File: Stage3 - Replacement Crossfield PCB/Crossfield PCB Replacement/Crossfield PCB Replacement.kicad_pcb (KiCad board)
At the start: 2 copper layers, 29 parts, among them P16-2 Power Amp Right, P25-2 Power Amp Left, P4-P24 Switch Mode PSU, P6-P18 12_Way_8-215079-2, Q1 BC549, Q2 BC549, Q3 BC549, Q4 BC549

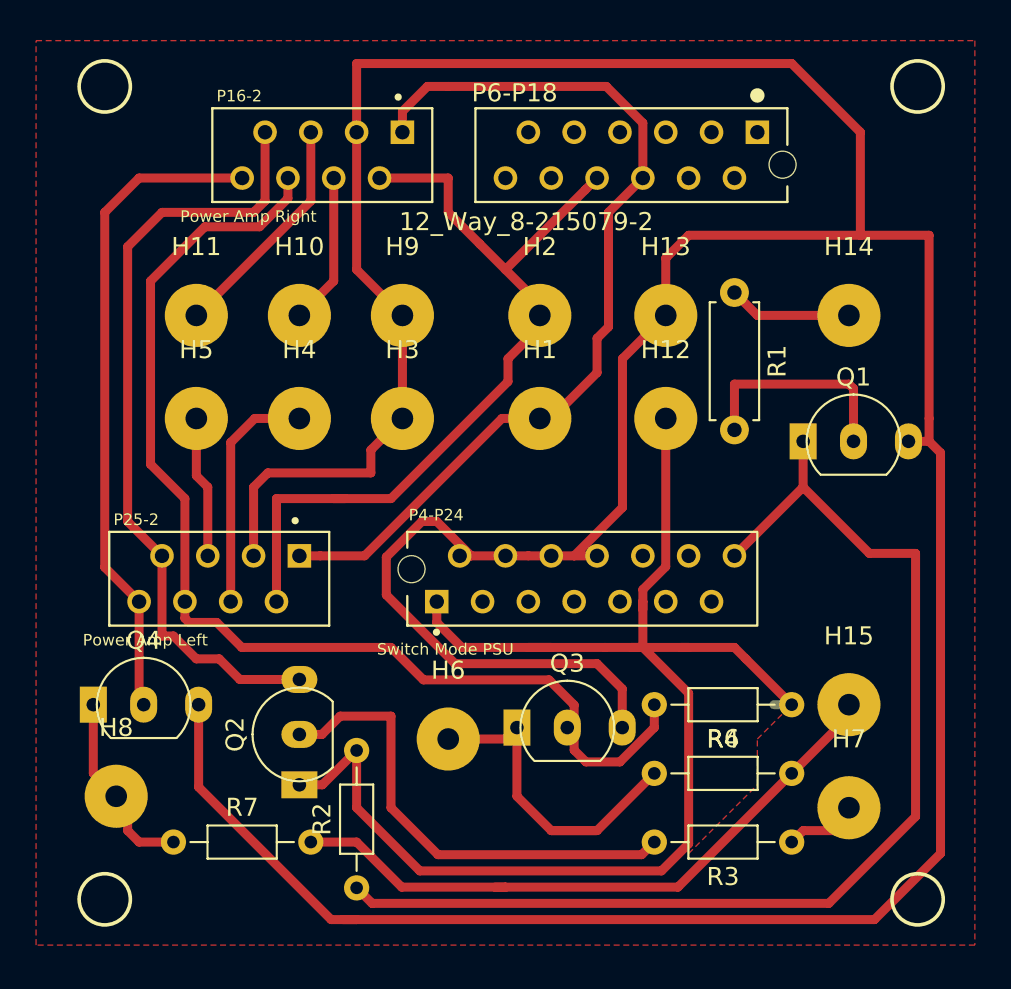
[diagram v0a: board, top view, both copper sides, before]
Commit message: Changed PCB now has USB PSU
The B&O PSU failed to provide enough mA for the raspberry. Now the switchmode PSU has been removed and replaced with a standard USB brick.
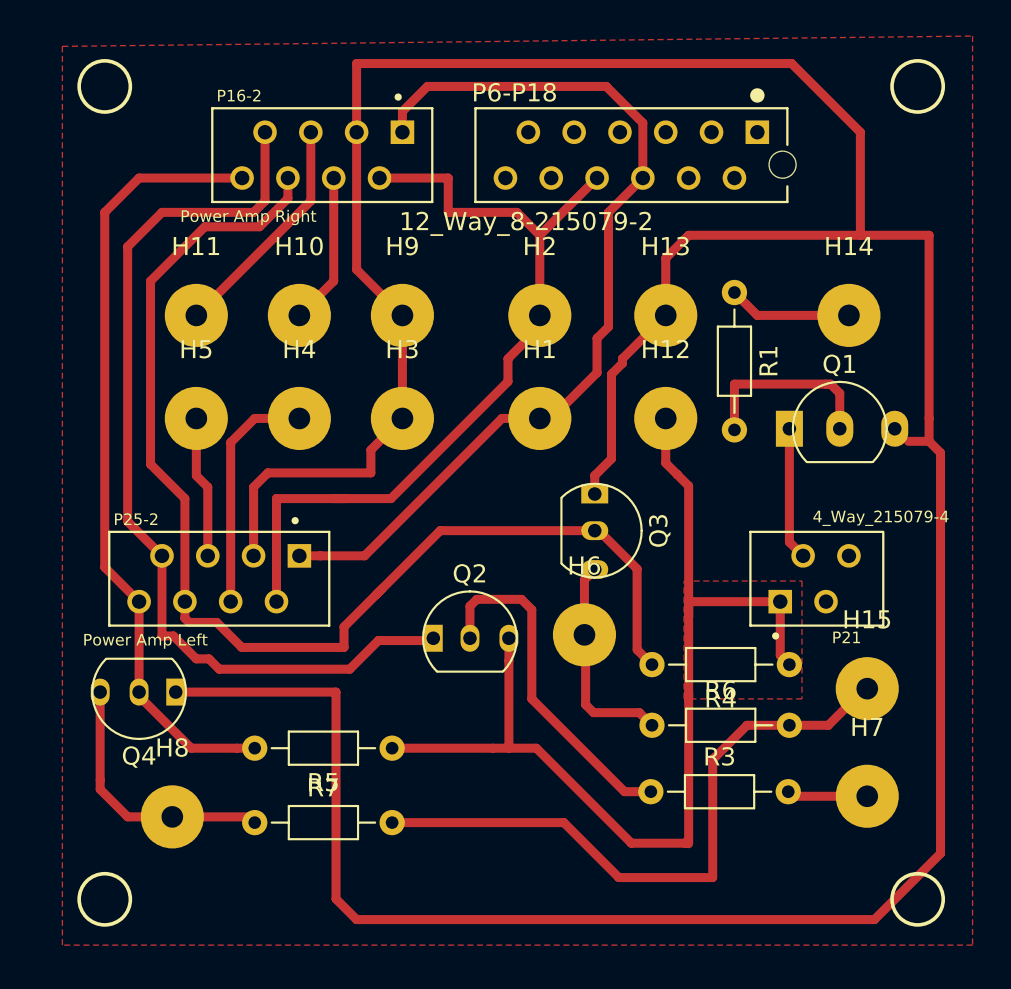
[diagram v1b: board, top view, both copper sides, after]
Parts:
- removed P4-P24: Switch Mode PSU, Connector_TE_215079_Series:TE_1-215079-4
- removed R2: 10k, Resistor_THT:R_Axial_DIN0204_L3.6mm_D1.6mm_P7.62mm_Horizontal
- added P21: 4_Way_215079-4, Connector_TE_215079_Series:TE_215079-4, F.Cu at (172.1, 109.9)
- added R5: 10k, Resistor_THT:R_Axial_DIN0204_L3.6mm_D1.6mm_P7.62mm_Horizontal, F.Cu at (146.1, 119.3)
- H6: value PLIM -> ~PLIM
- H8: value PFAIL -> ~PFAIL
- Q2, Q3, Q4: value BC549 -> BC557; footprint JamesParts:BC549_WideTerms -> JamesParts:bc557_WideLegs
- R1: footprint Resistor_THT:R_Axial_DIN0207_L6.3mm_D2.5mm_P7.62mm_Horizontal -> Resistor_THT:R_Axial_DIN0204_L3.6mm_D1.6mm_P7.62mm_Horizontal
- moved Q3 12.9 mm to (157.4, 105.9), turned to 270 degrees
- moved Q2 11.5 mm to (149.2, 113.2), turned to 0 degrees
- moved H6 9.51 mm to (156.8, 113.0)
- moved R3 8.30 mm to (160.5, 121.7), turned to 0 degrees
- moved R7 4.64 mm to (138.5, 123.4)
- moved Q4 3.87 mm to (133.3, 116.1), turned to 180 degrees
- moved H8 3.31 mm to (133.9, 123.1)
- moved R6 2.67 mm to (160.5, 118.0)
- moved R4 2.23 mm to (168.1, 114.6)
- moved H15 1.35 mm to (172.5, 116.0)
- moved H7 1.20 mm to (172.5, 121.9)
- moved Q1 1.03 mm to (168.1, 101.5)
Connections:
- Q2 pad 1: Net-(H12-Pad1) -> /PMUTE
- Q2 pad 3: /PMUTE -> Net-(H12-Pad1)
- Q3 pad 1: Net-(H6-Pad1) -> GND
- Q3 pad 3: GND -> Net-(H6-Pad1)
- Q4 pad 1: Net-(H8-Pad1) -> GND
- Q4 pad 3: GND -> Net-(H8-Pad1)
- R3 pad 1: Net-(H7-Pad1) -> Net-(Q2-Pad2)
- R3 pad 2: Net-(Q2-Pad2) -> Net-(H7-Pad1)
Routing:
- net Net-(P21-Pad2): track 63.6 -> 7.36 mm
- net GND: track 224.3 -> 191.8 mm
- net Net-(H12-Pad1): track 79.3 -> 58.8 mm
- net Net-(H6-Pad1): track 20.1 -> 12.3 mm
- net /PMUTE: track 43.5 -> 51.1 mm
- net Net-(Q2-Pad2): track 26.6 -> 19.4 mm
- net /~PFAIL: track 37.0 -> 44.1 mm
- net Net-(H8-Pad1): track 9.04 -> 14.7 mm
- net /~PLIM: track 63.0 -> 66.2 mm
- net Net-(H15-Pad1): track 36.3 -> 34.4 mm
- net Net-(Q1-Pad2): track 12.2 -> 10.6 mm
- net /-9V: track 47.5 -> 46.8 mm

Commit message: Fixed PCB to suit new pin out
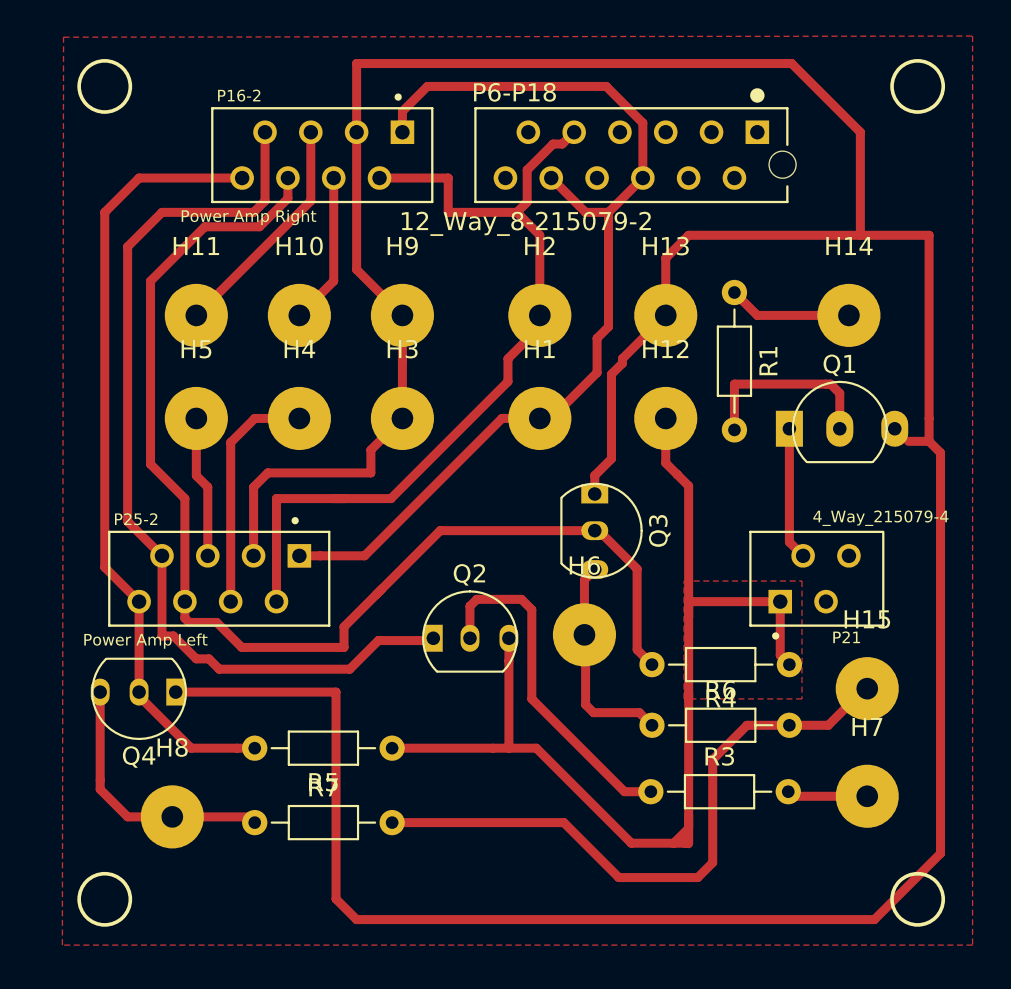
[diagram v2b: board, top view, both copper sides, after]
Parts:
- P6-P18: footprint TE_8-215079-2 -> Connector_TE_215079_Series:TE_8-215079-2
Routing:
- net /+9V: track 52.4 -> 56.4 mm
- net Net-(H12-Pad1): track 58.8 -> 60.6 mm
- net /-9V: track 46.8 -> 48.4 mm

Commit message: PCB tweaks
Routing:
- net /+9V: track 56.4 -> 56.9 mm
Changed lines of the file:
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@@
     (thickness 1.6)
     (drawings 4)
-    (tracks 189)
+    (tracks 191)
     (zones 0)
     (modules 29)
@@
   (segment (start 146.685 85.09) (end 146.685 83.936) (width 0.5) (layer F.Cu) (net 1))
   (segment (start 157.991922 82.55) (end 149.225 82.55) (width 0.5) (layer F.Cu) (net 1))
-  (segment (start 154.94 100.965) (end 157.48 98.425) (width 0.5) (layer F.Cu) (net 1))
-  (segment (start 157.48 98.425) (end 157.48 96.52) (width 0.5) (layer F.Cu) (net 1))
-  (segment (start 157.48 96.52) (end 158.115 95.885) (width 0.5) (layer F.Cu) (net 1))
   (segment (start 158.115 89.535) (end 160.02 87.63) (width 0.5) (layer F.Cu) (net 1))
-  (segment (start 158.115 95.885) (end 158.115 89.535) (width 0.5) (layer F.Cu) (net 1))
   (segment (start 156.845 89.535) (end 158.115 89.535) (width 0.5) (layer F.Cu) (net 1))
   (segment (start 154.94 87.63) (end 156.845 89.535) (width 0.5) (layer F.Cu) (net 1))
+  (segment (start 158.115 95.631) (end 158.115 96.139) (width 0.5) (layer F.Cu) (net 1))
+  (segment (start 158.115 95.631) (end 158.115 89.535) (width 0.5) (layer F.Cu) (net 1))
+  (segment (start 158.115 95.885) (end 158.115 95.631) (width 0.5) (layer F.Cu) (net 1))
+  (segment (start 158.115 96.139) (end 157.099 97.155) (width 0.5) (layer F.Cu) (net 1))
+  (segment (start 157.099 98.171) (end 154.305 100.965) (width 0.5) (layer F.Cu) (net 1))
+  (segment (start 157.099 97.155) (end 157.099 98.171) (width 0.5) (layer F.Cu) (net 1))
   (segment (start 139.7 111.125) (end 139.7 105.41) (width 0.5) (layer F.Cu) (net 10))
   (segment (start 152.539939 97.650061) (end 152.539939 98.920061) (width 0.5) (layer F.Cu) (net 10))

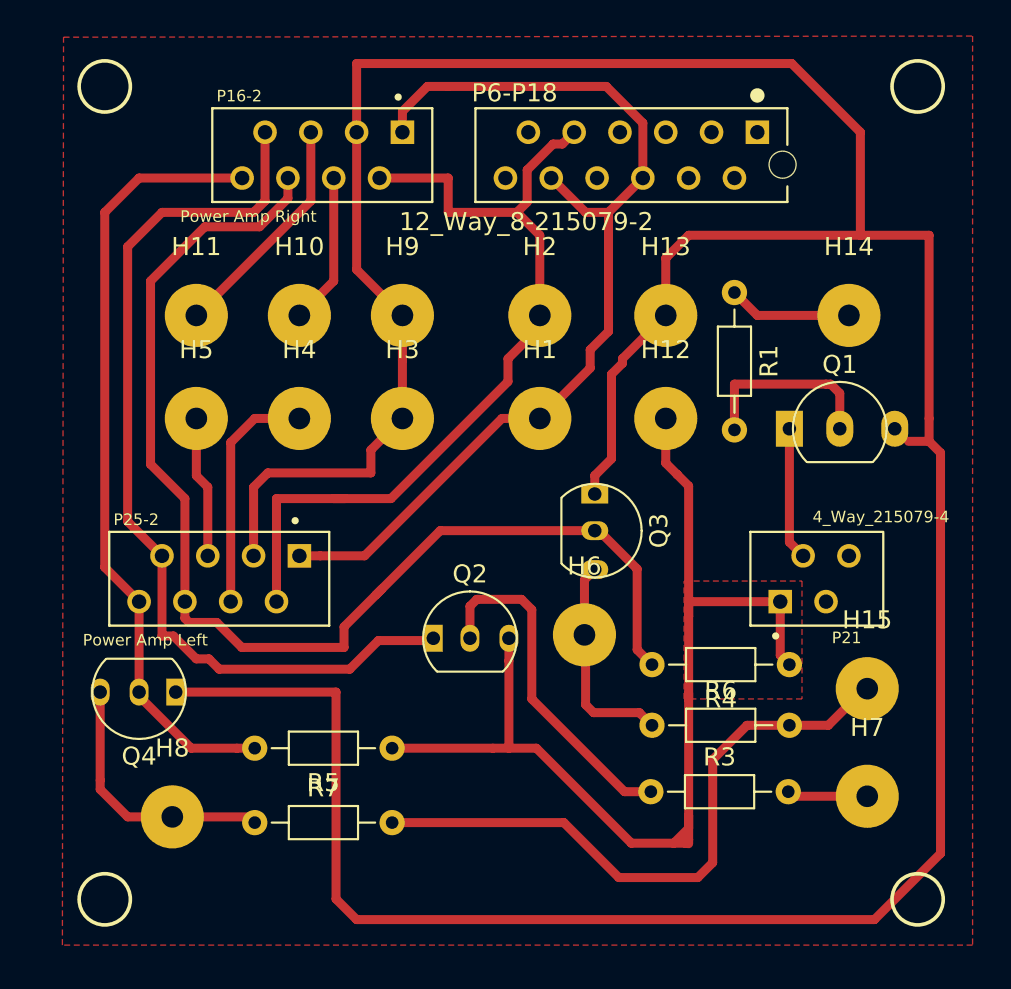
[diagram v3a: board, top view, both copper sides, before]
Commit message: Updated PCB following tests on PMUTE
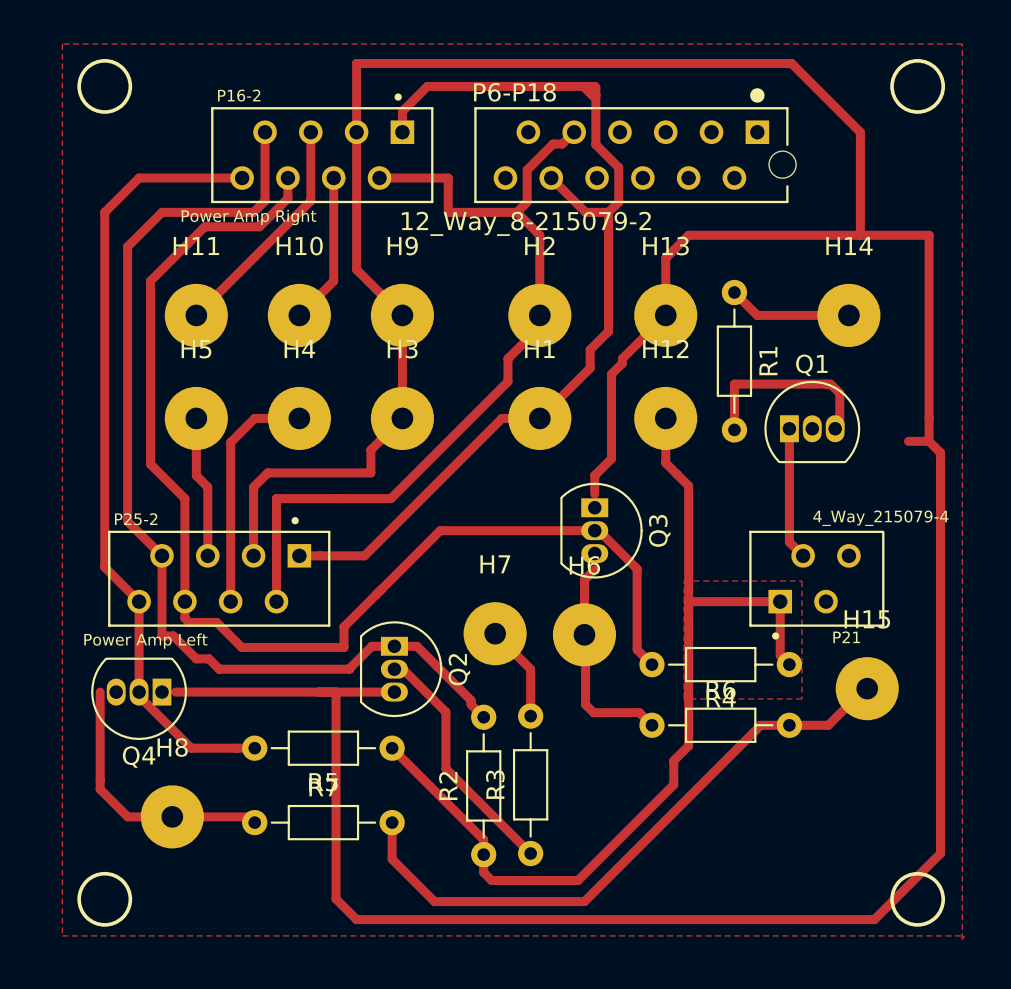
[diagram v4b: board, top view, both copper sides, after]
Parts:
- added R2: 10k, Resistor_THT:R_Axial_DIN0204_L3.6mm_D1.6mm_P7.62mm_Horizontal, F.Cu at (151.2, 125.2)
- H7: value PMUTE -> ~PMUTE
- P6-P18: footprint Connector_TE_215079_Series:TE_8-215079-2 -> TE_8-215079-2
- Q1: footprint JamesParts:BC549_WideTerms -> Package_TO_SOT_THT:TO-92_Inline
- Q2: value BC557 -> BC549; footprint JamesParts:bc557_WideLegs -> Package_TO_SOT_THT:TO-92_Inline
- Q3, Q4: footprint JamesParts:bc557_WideLegs -> Package_TO_SOT_THT:TO-92_Inline
- moved H7 22.5 mm to (151.8, 112.9)
- moved R3 7.50 mm to (153.8, 125.1), turned to 90 degrees
- moved Q2 2.95 mm to (146.2, 113.6), turned to 270 degrees
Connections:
- Q2 pad 3: Net-(H12-Pad1) -> GND
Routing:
- net Net-(H12-Pad1): track 60.6 -> 53.0 mm
- net Net-(Q2-Pad2): track 19.4 -> 13.6 mm
- net /PMUTE: track 51.1 -> 55.8 mm
- net GND: track 191.8 -> 196.0 mm
- net Net-(H15-Pad1): track 33.9 -> 32.9 mm
- net Net-(H7-Pad1): track 4.49 -> 5.39 mm
- net /+9V: track 56.9 -> 56.3 mm

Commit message: Widened legs on Transistors for easier working
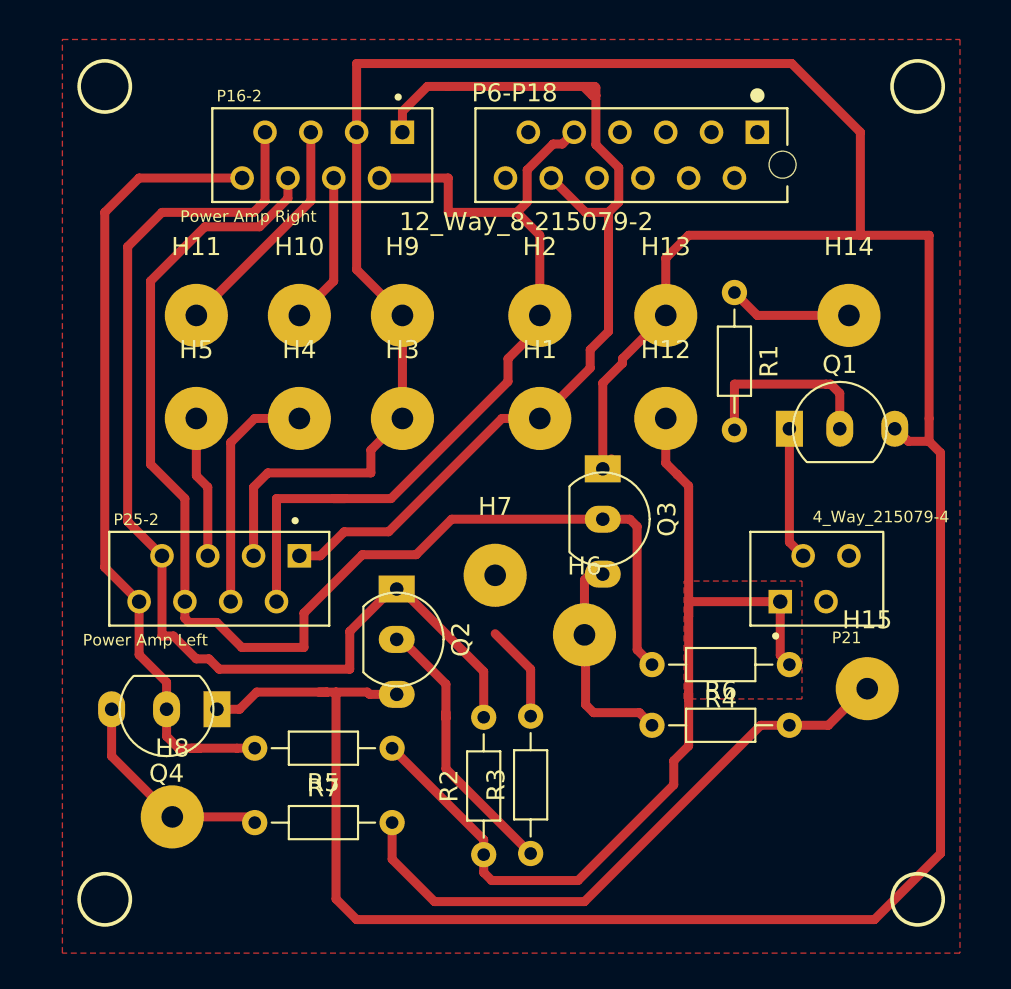
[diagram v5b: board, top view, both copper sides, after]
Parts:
- Q1, Q2, Q3, Q4: footprint Package_TO_SOT_THT:TO-92_Inline -> JamesParts:BC549_WideTerms
- moved H7 3.24 mm to (151.8, 109.7)
- moved Q4 3.19 mm to (136.4, 117.1)
- moved Q2 3.18 mm to (146.4, 110.4)
- moved Q3 2.20 mm to (157.8, 103.8)
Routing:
- net /PMUTE: track 55.8 -> 61.0 mm
- net Net-(H8-Pad1): track 14.7 -> 12.1 mm
- net /~PLIM: track 66.2 -> 68.1 mm
- net Net-(Q2-Pad2): track 13.6 -> 15.4 mm
- net GND: track 196.0 -> 194.5 mm

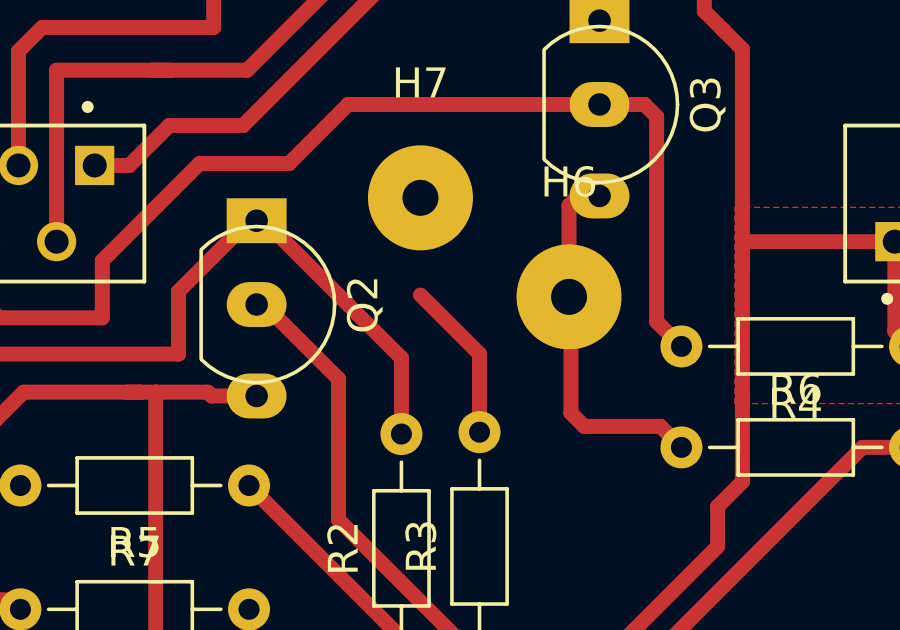
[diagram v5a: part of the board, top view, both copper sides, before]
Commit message: Fixed broken track
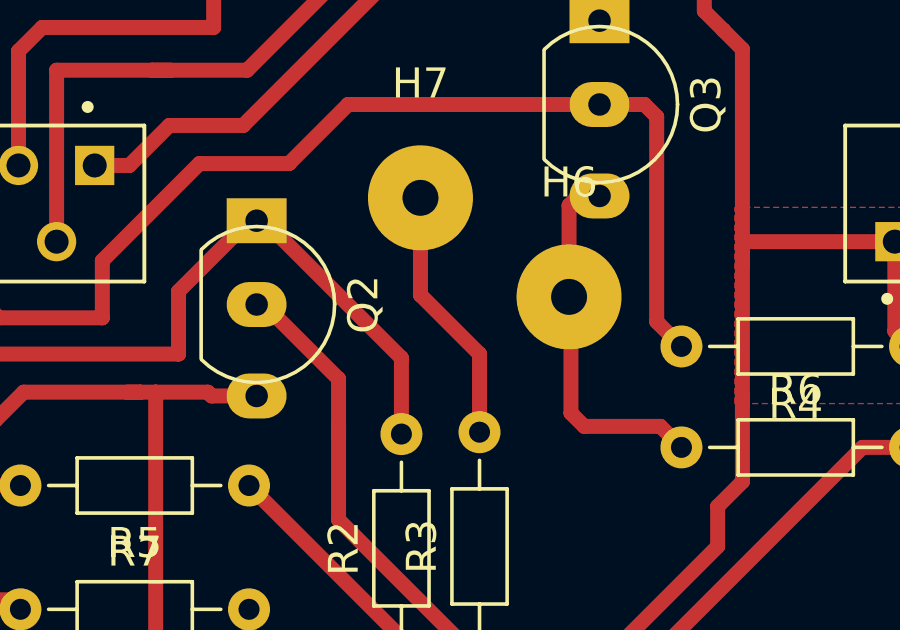
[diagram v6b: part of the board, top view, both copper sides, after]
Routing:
- net Net-(H7-Pad1): track 5.39 -> 8.63 mm
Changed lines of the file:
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@@
     (thickness 1.6)
     (drawings 4)
-    (tracks 202)
+    (tracks 203)
     (zones 0)
     (modules 30)
@@
   (segment (start 146.1135 123.3805) (end 146.1135 125.4125) (width 0.5) (layer F.Cu) (net 27))
   (segment (start 166.5605 117.983) (end 168.148 117.983) (width 0.5) (layer F.Cu) (net 27))
-  (segment (start 153.797 114.8715) (end 151.8285 112.903) (width 0.5) (layer F.Cu) (net 28))
-  (segment (start 153.797 117.475) (end 153.797 114.8715) (width 0.5) (layer F.Cu) (net 28))
+  (segment (start 153.797 114.8715) (end 153.797 117.475) (width 0.5) (layer F.Cu) (net 28))
+  (segment (start 151.8285 109.6645) (end 151.8285 112.903) (width 0.5) (layer F.Cu) (net 28))
+  (segment (start 151.8285 112.903) (end 153.797 114.8715) (width 0.5) (layer F.Cu) (net 28))
   (segment (start 168.148 107.823) (end 168.91 108.585) (width 0.5) (layer F.Cu) (net 29))
   (segment (start 168.148 101.5365) (end 168.148 107.823) (width 0.5) (layer F.Cu) (net 29))
